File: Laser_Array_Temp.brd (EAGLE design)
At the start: 93.5 x 160 mm, 83 parts, among them J1 22-23-2021, J10 22-23-2021, J11 22-23-2021, J12 22-23-2021, J2 22-23-2021, J3 22-23-2021, J4 22-23-2021, J5 22-23-2021, J6 22-23-2021, J7 22-23-2021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

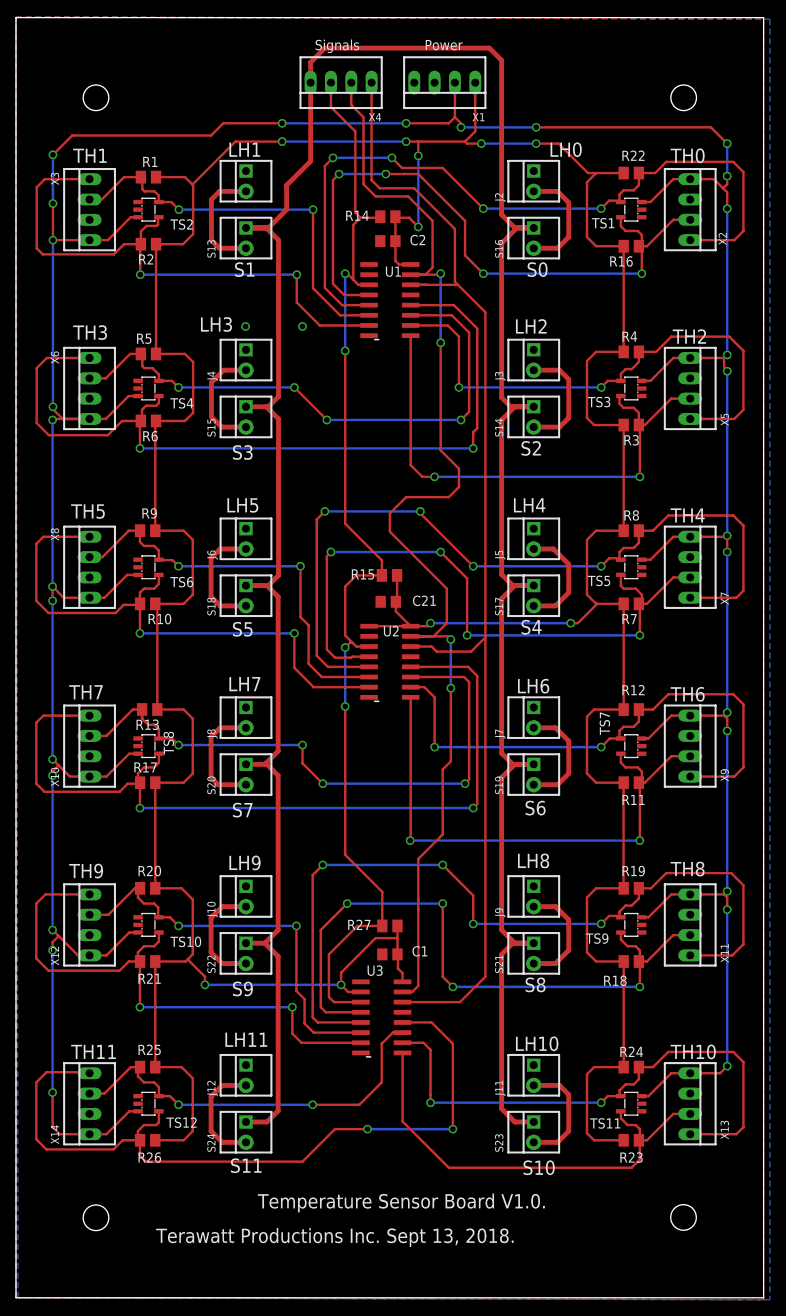
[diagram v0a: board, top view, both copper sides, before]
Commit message: Temperature_Sensor board, changed traces from 14 to 16, V1.1
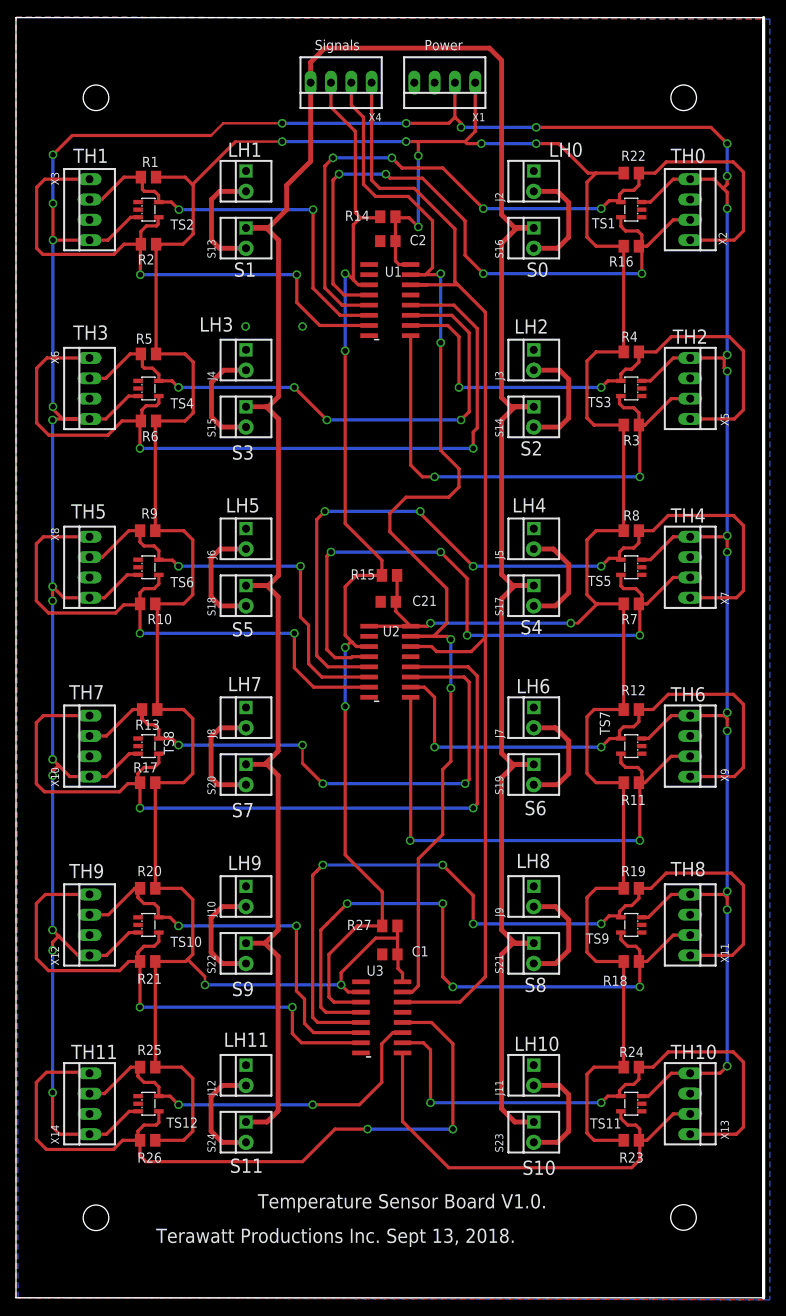
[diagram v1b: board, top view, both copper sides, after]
